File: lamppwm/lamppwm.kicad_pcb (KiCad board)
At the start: 2 copper layers, 36 x 36 mm, 15 parts, among them IC1 ATTINY85-S, P1 CONN_3X2, Q1 IRLML2246TRPBF, SW1 SWITCH-4, U1 AP7313

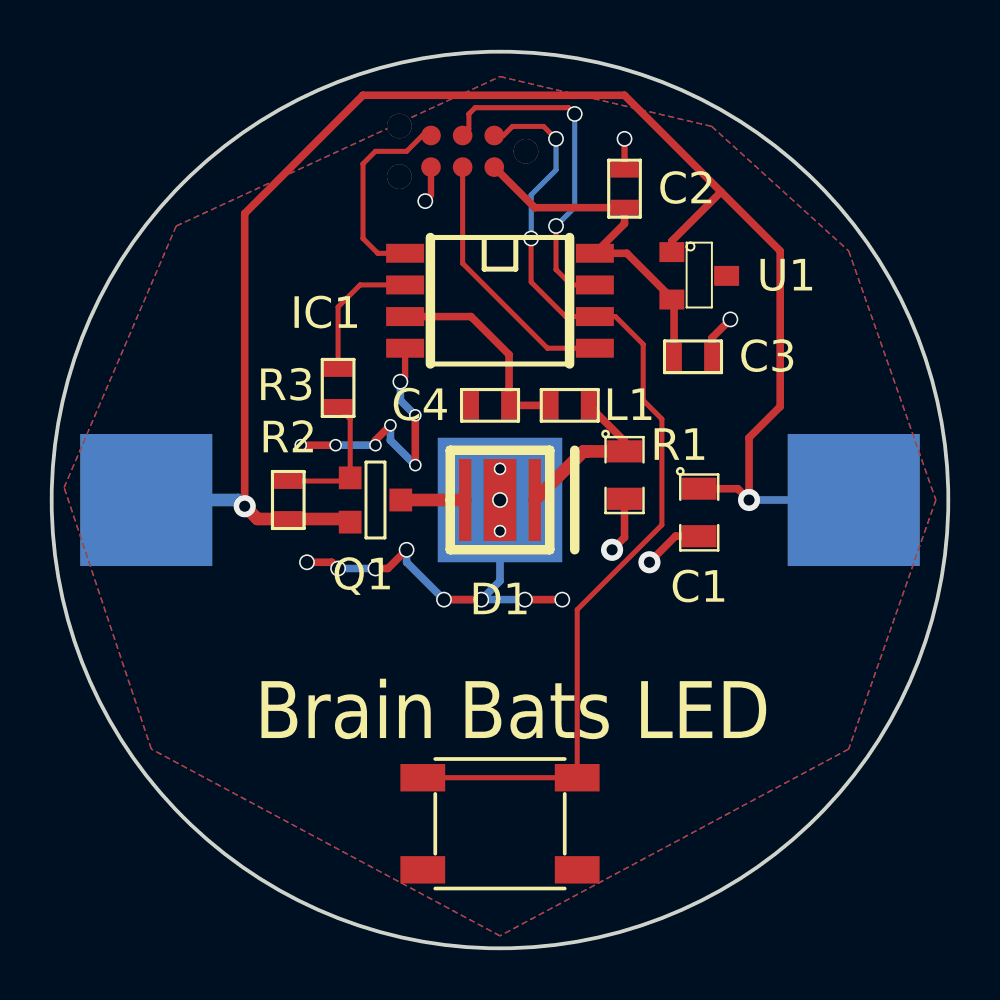
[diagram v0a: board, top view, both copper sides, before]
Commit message: lamppwm updates
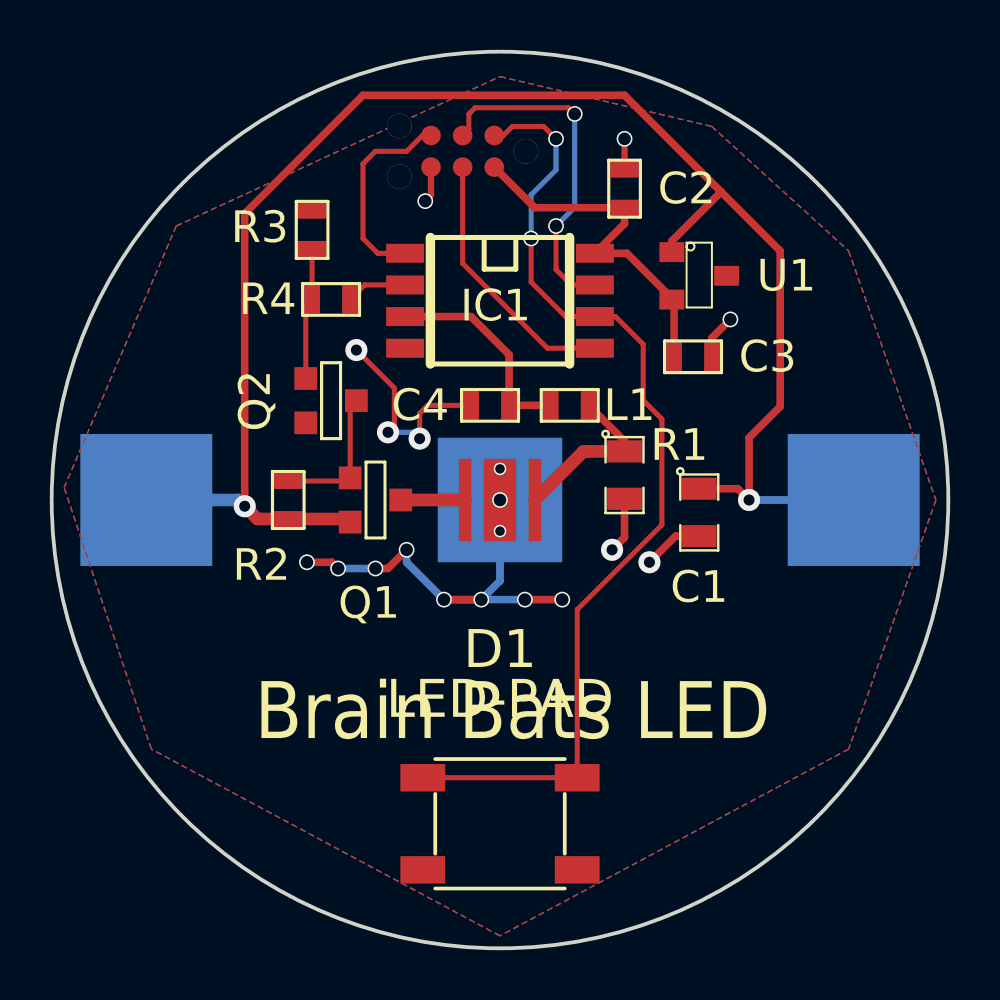
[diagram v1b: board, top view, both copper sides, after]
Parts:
- added Q2: NPN, SOT23EBC, F.Cu at (93.2, 96.0)
- added R4: 1K, SM0603, F.Cu at (93.2, 91.9)
- R3: value 100R -> 10K
- moved R3 6.43 mm to (92.5, 89.2)
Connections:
- Q1 pad G: N-000003 (its old number) -> N-000006
- R2 pad 2: N-000003 (its old number) -> N-000006
- R3 pad 1: N-000003 (its old number) -> N-000005
- R3 pad 2: /MOSFET -> GND
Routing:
- net N-000006: track 0.00 -> 5.74 mm
- net N-000003 (its old number): track 5.59 -> 0.00 mm
- net N-000005: track 0.00 -> 5.31 mm
- net /MOSFET: track 5.54 -> 2.45 mm
- net GND: track 42.9 -> 40.4 mm, vias 23 -> 19
